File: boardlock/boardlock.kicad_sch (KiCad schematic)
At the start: 52 parts, among them U1 ESP32-S3-WROOM-1

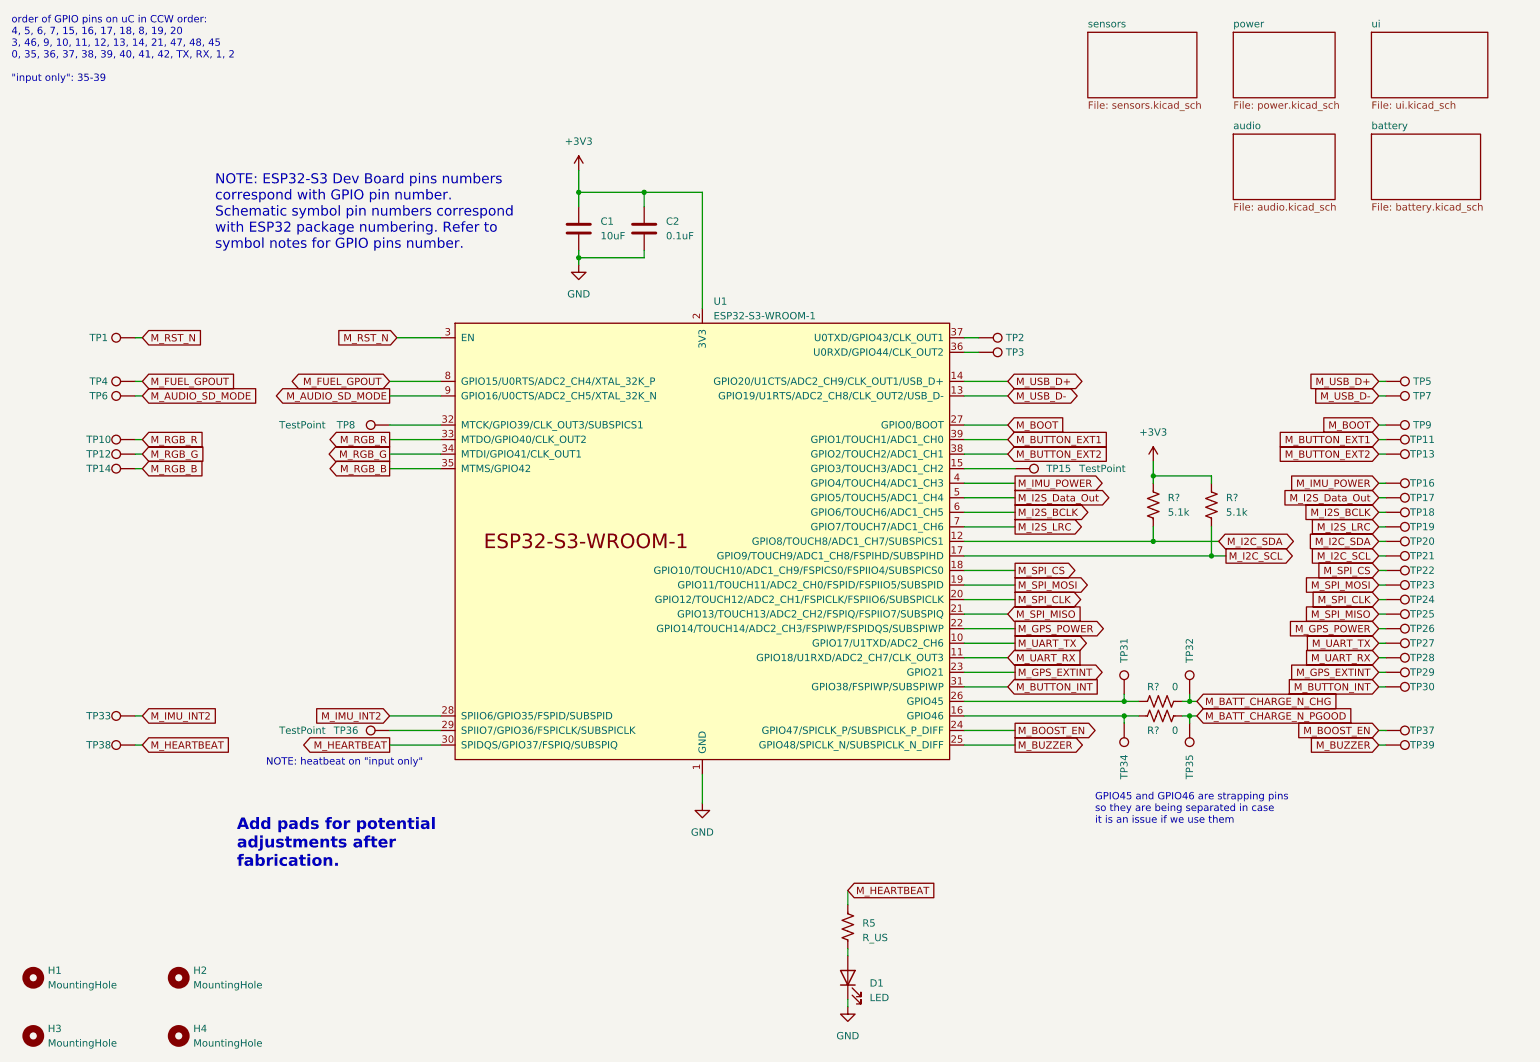
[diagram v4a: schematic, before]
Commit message: USB traces
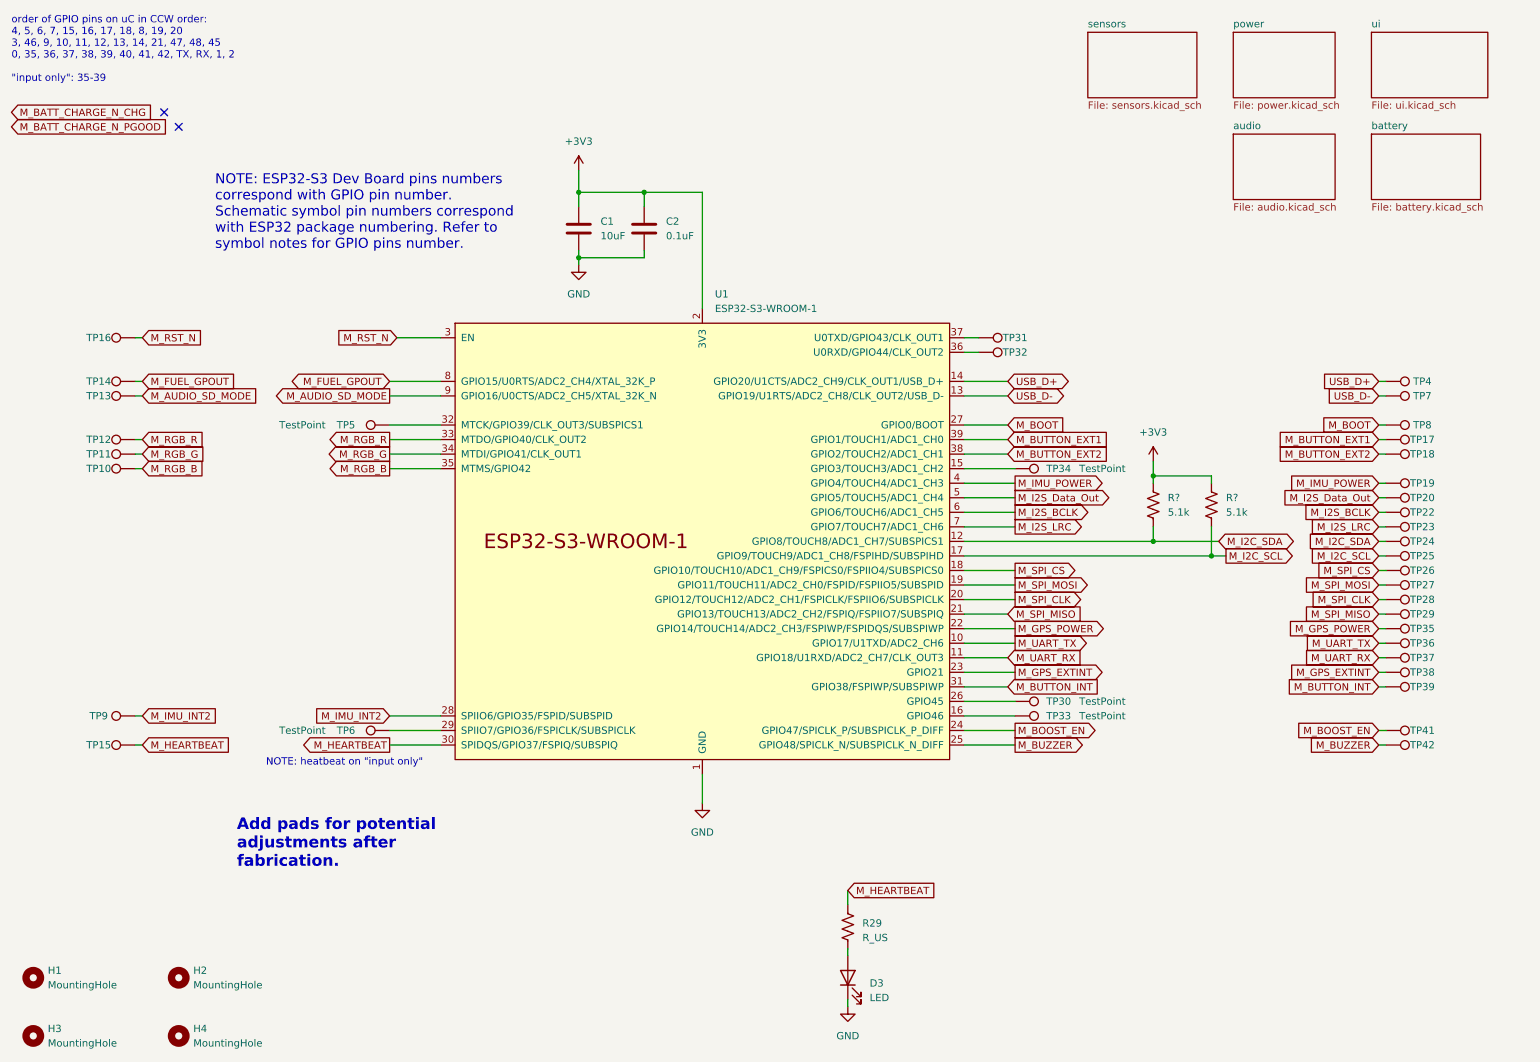
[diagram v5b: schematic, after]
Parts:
- removed R? (x2): 0, Resistor_SMD:R_0805_2012Metric_Pad1.20x1.40mm_HandSolder, symbol Device:R_US
- removed TP32, TP35: TestPoint, TestPoint:TestPoint_Pad_D1.0mm, symbol Connector:TestPoint
- removed U1: ESP32-S3-WROOM-1, espressif-kicad:ESP32-S3-WROOM-1, symbol Espressif:ESP32-S3-WROOM-1
- added U1: ESP32-S3-WROOM-1, PCM_Espressif:ESP32-S3-WROOM-1, symbol PCM_Espressif:ESP32-S3-WROOM-1
- H1, H2, H3, H4: footprint MountingHole:MountingHole_2.2mm_M2 -> (none)
- TP10: renamed from TP14; footprint TestPoint:TestPoint_Pad_D1.0mm -> (none)
- TP11: renamed from TP12; footprint TestPoint:TestPoint_Pad_D1.0mm -> (none)
- TP12: renamed from TP10; footprint TestPoint:TestPoint_Pad_D1.0mm -> (none)
- TP13: renamed from TP6; footprint TestPoint:TestPoint_Pad_D1.0mm -> (none)
- TP14: renamed from TP4; footprint TestPoint:TestPoint_Pad_D1.0mm -> (none)
- TP15: renamed from TP38; footprint TestPoint:TestPoint_Pad_D1.0mm -> (none)
- TP16: renamed from TP1; footprint TestPoint:TestPoint_Pad_D1.0mm -> (none)
- TP17: renamed from TP11; footprint TestPoint:TestPoint_Pad_D1.0mm -> (none)
- TP18: renamed from TP13; footprint TestPoint:TestPoint_Pad_D1.0mm -> (none)
- TP19: renamed from TP16; footprint TestPoint:TestPoint_Pad_D1.0mm -> (none)
- TP20: renamed from TP17; footprint TestPoint:TestPoint_Pad_D1.0mm -> (none)
- TP22: renamed from TP18; footprint TestPoint:TestPoint_Pad_D1.0mm -> (none)
- TP23: renamed from TP19; footprint TestPoint:TestPoint_Pad_D1.0mm -> (none)
- TP24: renamed from TP20; footprint TestPoint:TestPoint_Pad_D1.0mm -> (none)
- TP25: renamed from TP21; footprint TestPoint:TestPoint_Pad_D1.0mm -> (none)
- TP26: renamed from TP22; footprint TestPoint:TestPoint_Pad_D1.0mm -> (none)
- TP27: renamed from TP23; footprint TestPoint:TestPoint_Pad_D1.0mm -> (none)
- TP28: renamed from TP24; footprint TestPoint:TestPoint_Pad_D1.0mm -> (none)
- TP29: renamed from TP25; footprint TestPoint:TestPoint_Pad_D1.0mm -> (none)
- TP30: renamed from TP31; footprint TestPoint:TestPoint_Pad_D1.0mm -> TestPoint:TestPoint_Plated_Hole_D3.0mm
- TP31: renamed from TP2; footprint TestPoint:TestPoint_Pad_D1.0mm -> (none)
- TP32: renamed from TP3; footprint TestPoint:TestPoint_Pad_D1.0mm -> (none)
- TP33: renamed from TP34; footprint TestPoint:TestPoint_Pad_D1.0mm -> TestPoint:TestPoint_Plated_Hole_D3.0mm
- TP34: renamed from TP15; footprint TestPoint:TestPoint_Pad_D1.0mm -> TestPoint:TestPoint_Plated_Hole_D3.0mm
- TP35: renamed from TP26; footprint TestPoint:TestPoint_Pad_D1.0mm -> (none)
- TP36: renamed from TP27; footprint TestPoint:TestPoint_Pad_D1.0mm -> (none)
- TP37: renamed from TP28; footprint TestPoint:TestPoint_Pad_D1.0mm -> (none)
- TP38: renamed from TP29; footprint TestPoint:TestPoint_Pad_D1.0mm -> (none)
- TP39: renamed from TP30; footprint TestPoint:TestPoint_Pad_D1.0mm -> (none)
- TP4: renamed from TP5; footprint TestPoint:TestPoint_Pad_D1.0mm -> (none)
- TP41: renamed from TP37; footprint TestPoint:TestPoint_Pad_D1.0mm -> (none)
- TP42: renamed from TP39; footprint TestPoint:TestPoint_Pad_D1.0mm -> (none)
- TP5: renamed from TP8; footprint TestPoint:TestPoint_Pad_D1.0mm -> TestPoint:TestPoint_Plated_Hole_D3.0mm
- TP7: footprint TestPoint:TestPoint_Pad_D1.0mm -> (none)
- TP8: renamed from TP9; footprint TestPoint:TestPoint_Pad_D1.0mm -> (none)
- TP9: renamed from TP33; footprint TestPoint:TestPoint_Pad_D1.0mm -> (none)
- renumbered D1 to D3, R5 to R29, TP36 to TP6
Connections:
- net +3V3: now also U1.2 (3V3)
- net GND: now also U1.1 (GND), U1.40 (GND), U1.41 (GND)
- net M_AUDIO_SD_MODE: now also U1.9 (GPIO16/U0CTS/ADC2_CH5/XTAL_32K_N)
- net M_BOOST_EN: now also U1.24 (GPIO47/SPICLK_P/SUBSPICLK_P_DIFF)
- net M_BOOT: now also U1.27 (GPIO0/BOOT)
- net M_BUTTON_EXT1: now also U1.39 (GPIO1/TOUCH1/ADC1_CH0)
- net M_BUTTON_EXT2: now also U1.38 (GPIO2/TOUCH2/ADC1_CH1)
- net M_BUTTON_INT: now also U1.31 (GPIO38/FSPIWP/SUBSPIWP)
- net M_BUZZER: now also U1.25 (GPIO48/SPICLK_N/SUBSPICLK_N_DIFF)
- net M_FUEL_GPOUT: now also U1.8 (GPIO15/U0RTS/ADC2_CH4/XTAL_32K_P)
- net M_GPS_EXTINT: now also U1.23 (GPIO21)
- net M_GPS_POWER: now also U1.22 (GPIO14/TOUCH14/ADC2_CH3/FSPIWP/FSPIDQS/SUBSPIWP)
- net M_HEARTBEAT: now also U1.30 (SPIDQS/GPIO37/FSPIQ/SUBSPIQ)
- net M_I2C_SCL: now also U1.17 (GPIO9/TOUCH9/ADC1_CH8/FSPIHD/SUBSPIHD)
- net M_I2C_SDA: now also U1.12 (GPIO8/TOUCH8/ADC1_CH7/SUBSPICS1)
- net M_I2S_BCLK: now also U1.6 (GPIO6/TOUCH6/ADC1_CH5)
- net M_I2S_Data_Out: now also U1.5 (GPIO5/TOUCH5/ADC1_CH4)
- net M_I2S_LRC: now also U1.7 (GPIO7/TOUCH7/ADC1_CH6)
- net M_IMU_INT2: now also U1.28 (SPIIO6/GPIO35/FSPID/SUBSPID)
- net M_IMU_POWER: now also U1.4 (GPIO4/TOUCH4/ADC1_CH3)
- net M_RGB_B: now also U1.35 (MTMS/GPIO42)
- net M_RGB_G: now also U1.34 (MTDI/GPIO41/CLK_OUT1)
- net M_RGB_R: now also U1.33 (MTDO/GPIO40/CLK_OUT2)
- net M_RST_N: now also U1.3 (EN)
- net M_SPI_CLK: now also U1.20 (GPIO12/TOUCH12/ADC2_CH1/FSPICLK/FSPIIO6/SUBSPICLK)
- net M_SPI_CS: now also U1.18 (GPIO10/TOUCH10/ADC1_CH9/FSPICS0/FSPIIO4/SUBSPICS0)
- net M_SPI_MISO: now also U1.21 (GPIO13/TOUCH13/ADC2_CH2/FSPIQ/FSPIIO7/SUBSPIQ)
- net M_SPI_MOSI: now also U1.19 (GPIO11/TOUCH11/ADC2_CH0/FSPID/FSPIIO5/SUBSPID)
- net M_UART_RX: now also U1.11 (GPIO18/U1RXD/ADC2_CH7/CLK_OUT3)
- net M_UART_TX: now also U1.10 (GPIO17/U1TXD/ADC2_CH6)
- net at TP31.1: now also U1.37 (U0TXD/GPIO43/CLK_OUT1)
- net at TP33.1: now also U1.16 (GPIO46)
- net at TP34.1: now also U1.15 (GPIO3/TOUCH3/ADC1_CH2)
- net at TP6.1: now also U1.29 (SPIIO7/GPIO36/FSPICLK/SUBSPICLK)
- net at TP30.1: now also U1.26 (GPIO45)
- net at TP32.1: now also U1.36 (U0RXD/GPIO44/CLK_OUT2)
- net at TP5.1: now also U1.32 (MTCK/GPIO39/CLK_OUT3/SUBSPICS1)
- net M_USB_D+ renamed USB_D+
- net USB_D+: now also U1.14 (GPIO20/U1CTS/ADC2_CH9/CLK_OUT1/USB_D+)
- net M_USB_D- renamed USB_D-
- net USB_D-: now also U1.13 (GPIO19/U1RTS/ADC2_CH8/CLK_OUT2/USB_D-)
- no-connect marks 0 -> 2
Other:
- note removed: "GPIO45 and GPIO46 are strapping pins so they are being separated in case it is an issue if we use them"
- moved on the sheet: TP30, TP33

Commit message: correcting old schematic and footprints
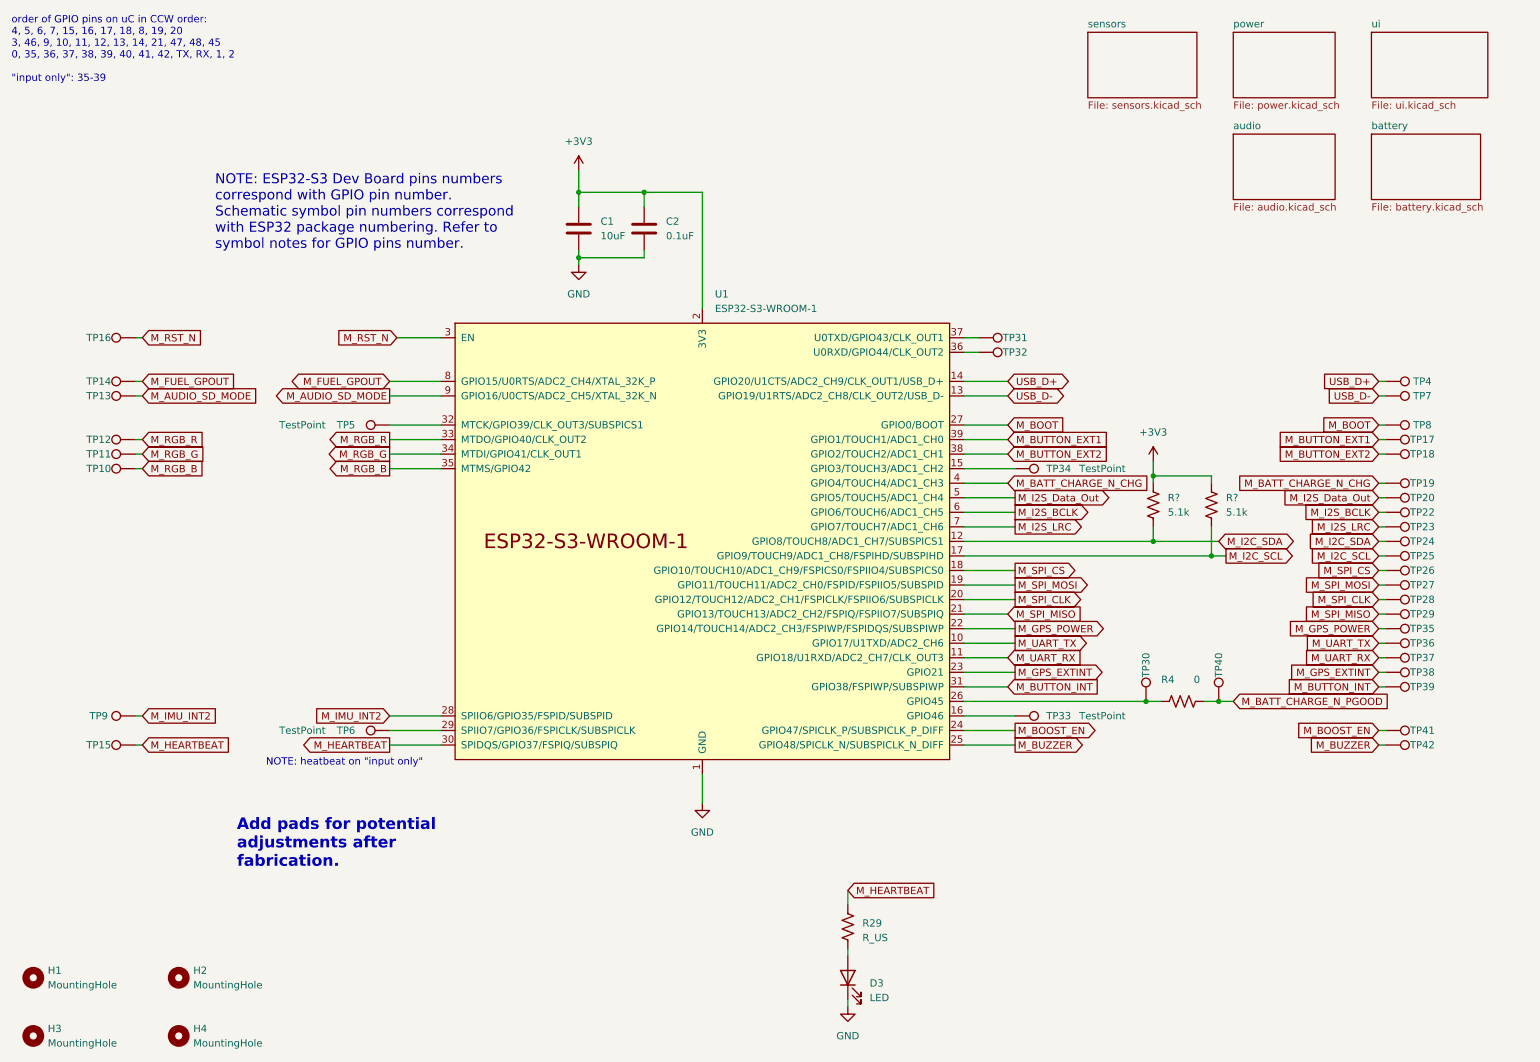
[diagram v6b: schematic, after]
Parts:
- added R4: 0, Resistor_SMD:R_0805_2012Metric_Pad1.20x1.40mm_HandSolder, symbol Device:R_US
- added TP40: TestPoint, TestPoint:TestPoint_Pad_D1.0mm, symbol Connector:TestPoint
- H1, H2, H3, H4: footprint (none) -> MountingHole:MountingHole_2.2mm_M2
- TP10, TP11, TP12, TP13, TP14, TP15, TP16, TP17, TP18, TP19, TP20, TP22, TP23, TP24, TP25, TP26, TP27, TP28, TP29, TP31, TP32, TP35, TP36, TP37, TP38, TP39, TP4, TP41, TP42, TP7, TP8, TP9: footprint (none) -> TestPoint:TestPoint_Pad_D1.0mm
- TP30, TP33, TP34, TP5: footprint TestPoint:TestPoint_Plated_Hole_D3.0mm -> TestPoint:TestPoint_Pad_D1.0mm
- U1: footprint PCM_Espressif:ESP32-S3-WROOM-1 -> espressif-kicad:ESP32-S3-WROOM-1
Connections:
- net M_IMU_POWER is gone; now on net M_BATT_CHARGE_N_CHG: TP19.1, U1.4 (GPIO4/TOUCH4/ADC1_CH3)
- net M_BATT_CHARGE_N_PGOOD: now also R4.2, TP40.1
- net at TP30.1, U1.26 (GPIO45): now also R4.1
- no-connect marks 2 -> 0

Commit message: pcb work
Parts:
- added H5: MountingHole, MountingHole:MountingHole_2.2mm_M2, symbol Mechanical:MountingHole
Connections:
- net M_BATT_CHARGE_N_CHG: now also U1.22 (GPIO14/TOUCH14/ADC2_CH3/FSPIWP/FSPIDQS/SUBSPIWP); no longer U1.4 (GPIO4/TOUCH4/ADC1_CH3)
- net M_GPS_POWER: now also U1.4 (GPIO4/TOUCH4/ADC1_CH3); no longer U1.22 (GPIO14/TOUCH14/ADC2_CH3/FSPIWP/FSPIDQS/SUBSPIWP)
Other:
- moved on the sheet: TP19, TP35

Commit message: more pcb stuff
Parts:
- renumbered D3 to D1, R4 to R3, R29 to R4, TP16 to TP1, TP12 to TP10, TP17 to TP11, TP11 to TP12, TP18 to TP13, TP10 to TP14, TP34 to TP15, TP35 to TP16, TP20 to TP17, TP22 to TP18, TP23 to TP19, TP31 to TP2, TP24 to TP20, TP25 to TP21, TP26 to TP22, TP27 to TP23, TP28 to TP24, TP29 to TP25, TP19 to TP26, TP36 to TP27, TP37 to TP28, TP38 to TP29, TP32 to TP3, TP39 to TP30, TP30 to TP31, TP40 to TP32, TP9 to TP33, TP33 to TP34, TP6 to TP35, TP41 to TP36, TP15 to TP37, TP42 to TP38, TP14 to TP4, TP4 to TP5, TP13 to TP6, TP5 to TP8, TP8 to TP9
